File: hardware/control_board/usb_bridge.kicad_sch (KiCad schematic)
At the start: 1 part, among them U2 FT232H

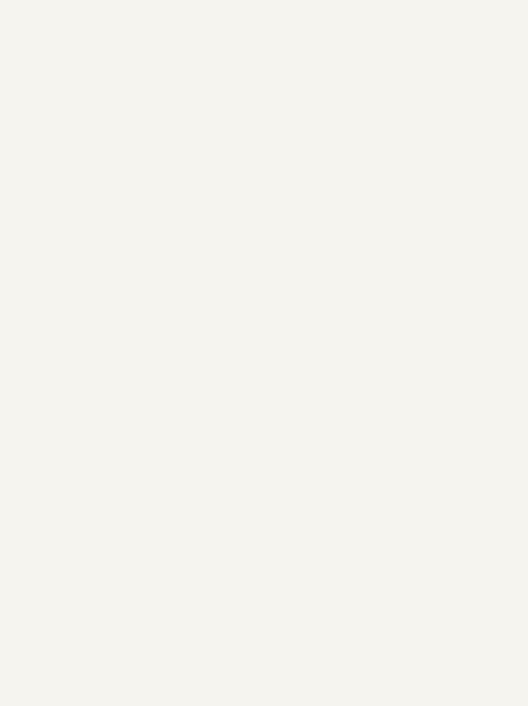
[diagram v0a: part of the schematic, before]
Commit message: added symbols and footprints
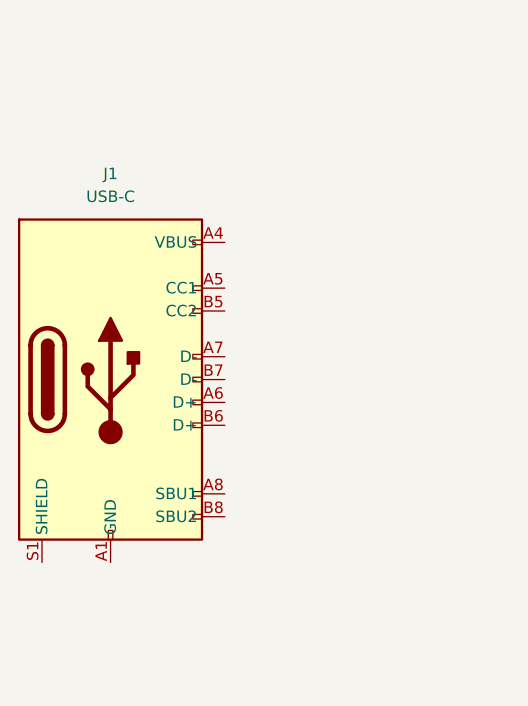
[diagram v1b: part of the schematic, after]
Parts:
- added J1: USB-C, Library:USB-C, symbol Library:USB-C
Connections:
- new net: J1.A1 (GND), J1.A12 (GND), J1.B1 (GND), J1.B12 (GND)
- new net: J1.A4 (VBUS), J1.A9 (VBUS), J1.B4 (VBUS), J1.B9 (VBUS)
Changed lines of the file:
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@@
 	(paper "A4")
+	(symbol
+		(lib_id "Library:USB-C")
+		(at 49.53 86.36 0)
+		(unit 1)
+		(exclude_from_sim no)
+		(in_bom yes)
+		(on_board yes)
+		(dnp no)
+		(fields_autoplaced yes)
+		(property "Reference" "J1"
+			(at 49.53 63.5 0)
+			(effects
+				(font
+					(size 1.27 1.27)
+				)
+			)
+		)
+		(property "Value" "USB-C"
+			(at 49.53 66.04 0)
+			(effects
+				(font
+					(size 1.27 1.27)
+				)
+			)
+		)
+		(property "Footprint" "Library:USB-C"
+			(at 49.022 115.316 0)
+			(effects
+				(font
+					(size 1.27 1.27)
+				)
+				(hide yes)
+			)
+		)
+		(property "Datasheet" ""
+			(at 49.022 115.316 0)
+			(effects
+				(font
+					(size 1.27 1.27)
+				)
+				(hide yes)
+			)
+		)
+		(property "Description" "USB-C Jack"
+			(at 49.53 117.602 0)
+			(effects
+				(font
+					(size 1.27 1.27)
+				)
+				(hide yes)
+			)
+		)
+		(pin "A7"
+		)
+		(pin "B12"
+		)
+		(pin "S1"
+		)
+		(pin "A9"
+		)
+		(pin "B4"
+		)
+		(pin "A8"
+		)
+		(pin "B8"
+		)
+		(pin "B1"
+		)
+		(pin "A12"
+		)
+		(pin "A1"
+		)
+		(pin "B5"
+		)
+		(pin "B7"
+		)
+		(pin "A4"
+		)
+		(pin "B9"
+		)
+		(pin "A6"
+		)
+		(pin "B6"
+		)
+		(pin "A5"
+		)
+		(instances
+			(project ""
+				(path "/acca031a-6f31-41bd-bf7c-a4abb4bf7051/b389096f-601d-4fb6-9b0a-9485f91135c9"
+					(reference "J1")
+					(unit 1)
+				)
+			)
+		)
+	)
 	(symbol
 		(lib_id "Interface_USB:FT232H")

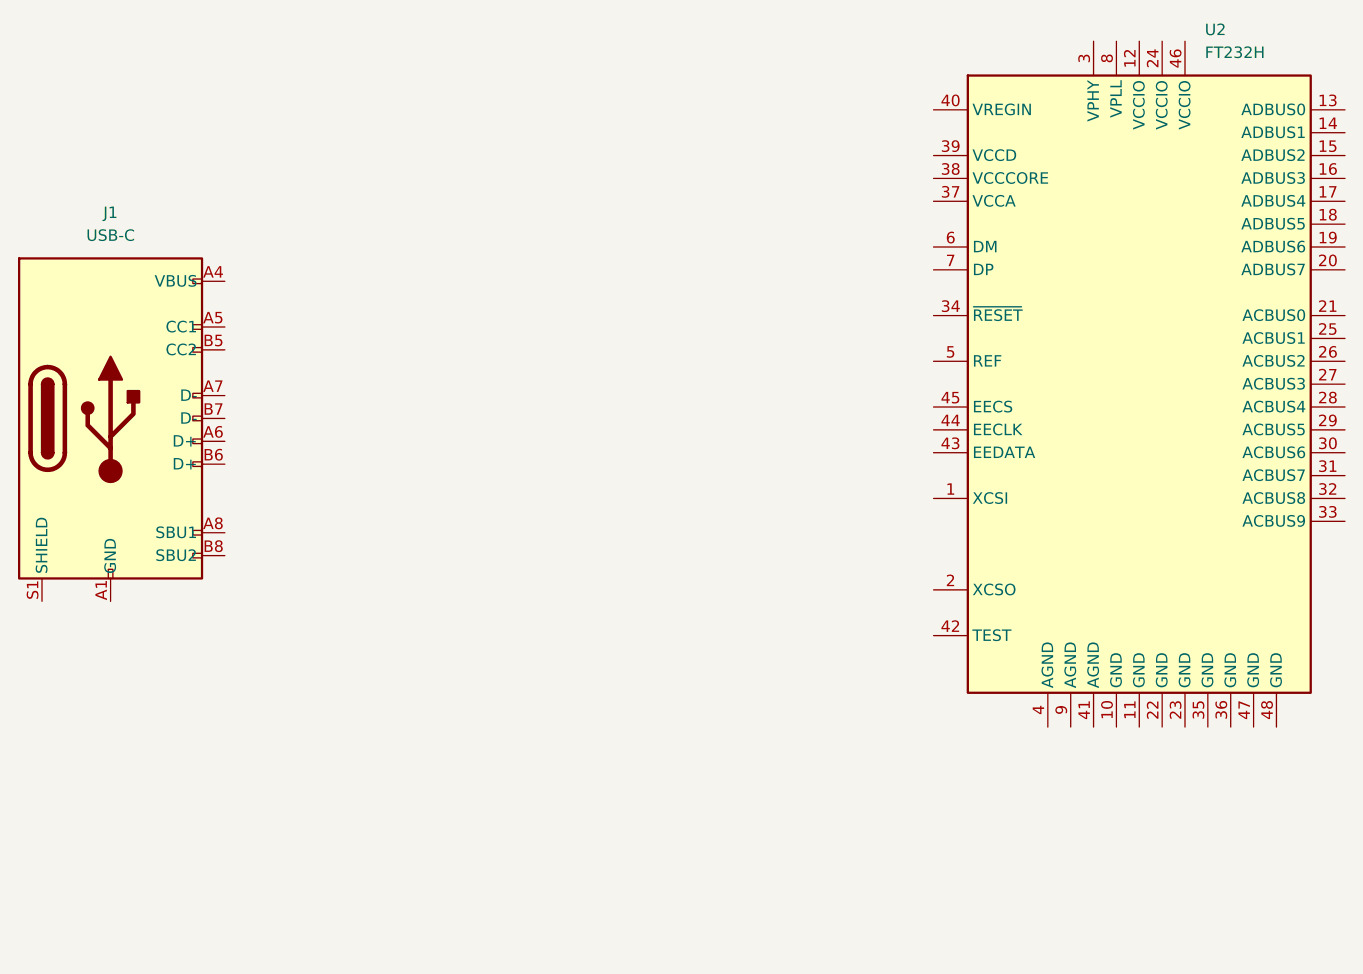
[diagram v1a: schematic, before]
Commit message: added components to uart bridge
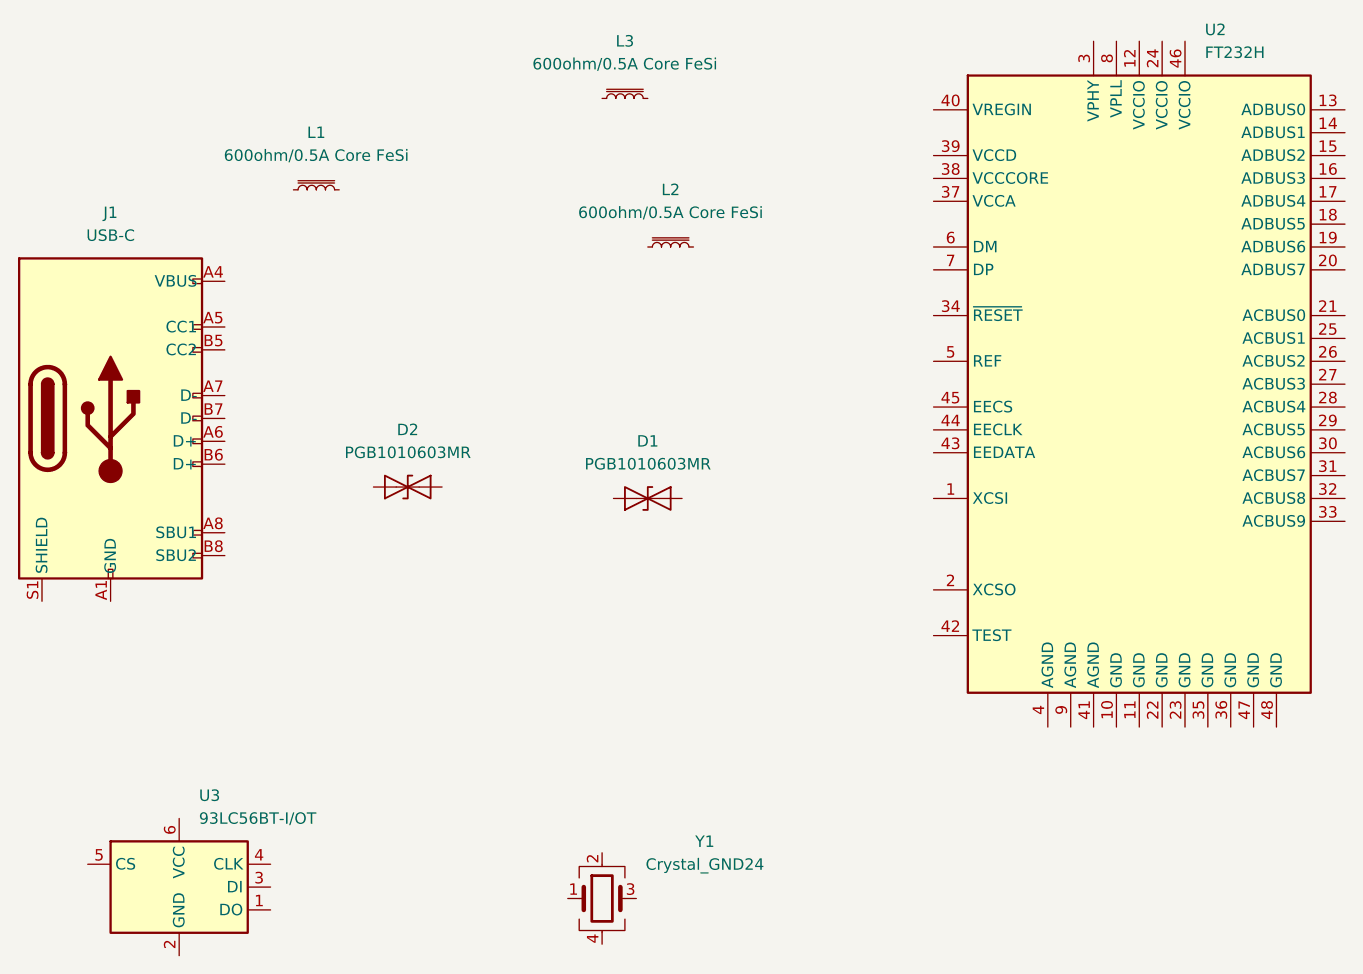
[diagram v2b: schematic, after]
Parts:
- added D1, D2: PGB1010603MR, Diode_SMD:D_0603_1608Metric, symbol Diode:SMAJ5.0CA
- added L1, L2, L3: 600ohm/0.5A Core FeSi, Inductor_SMD:L_0603_1608Metric, symbol Device:L_Iron_Small
- added U3: 93LC56BT-I/OT, Package_TO_SOT_SMD:SOT-23-6, symbol Memory_EEPROM:93LCxxAxxOT
- added Y1: Crystal_GND24, Crystal:Crystal_SMD_SeikoEpson_FA238V-4Pin_3.2x2.5mm, symbol Device:Crystal_GND24
- U2: footprint (none) -> Package_DFN_QFN:NXP_LQFN-48-1EP_7x7mm_P0.5mm_EP3.5x3.5mm_16xMask0.45x0.45
